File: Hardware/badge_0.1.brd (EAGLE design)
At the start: 100 x 50 mm, 60 parts, among them CON1 PH_2, IC1 CP2102, SW2 MK12C02, U1 SMBT2222A, U2 SMBT2222A, U4 MCP73832T-2DCI/OT

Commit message: okey dokey
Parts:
- removed R2, R3: 12K, SparkFun-Passives:0805
- removed U1, U2: SMBT2222A, badge:SOT95P290X110-3N
- added IC2: PIMH9, badge:SOT457
- added J7: 2X6 FEMALE, SparkFun-Connectors:2X6
- added JP2, JP3, JP4, JP6: JUMPER-PAD-2-NOJELLY, SparkFun-Passives:JELLYPAD-JUMPER-2-NO_NO_SILK
- J1: device SparkFun-Connectors:1X04 -> SparkFun-Connectors:1X03
- JP1: value (none) -> JUMPER-PAD-2-NOJELLY; device pinhead:1X06 -> SparkFun-Passives:JELLYPAD-JUMPER-2-NO_NO_SILK
- moved JP1 6.16 mm to (44.7, 35.6)
- moved D1 2.06 mm to (56.8, 44.8)
- moved C3 1.83 mm to (54.4, 8.57)
- moved IC1 1.75 mm to (52.4, 13.6)
- moved U$11 1.35 mm to (59.5, 37.0)
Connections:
- removed net N$10: R2.1, U1.1
- removed net N$3: R3.1, U2.1
- removed net S_!SUSP: IC1.11, J1.4
- new net DTR: IC2.P$2, IC2.P$4, J7.12, JP1.1
- new net RTS: IC2.P$1, IC2.P$5, J7.6, JP6.1
- new net S_RX: IC1.25, J2.6, J7.9, JP2.2
- new net S_TX: IC1.26, J2.5, J7.7, JP3.2
- net 5V: now also J7.4, JP4.2
- net GND: now also J7.1, J7.2; no longer JP1.1
- net GPIO0: now also IC2.P$3; no longer U1.3
- net RESET: now also IC2.P$6; no longer U2.3
- net RX: now also J7.8, JP3.1; no longer IC1.25, J2.6, JP1.4
- net S_DTR: now also J7.11, JP1.2; no longer JP1.6, R3.2, U1.2
- net S_RTS: now also J7.5, JP6.2; no longer JP1.3, R2.2, U2.2
- net TX: now also J7.10, JP2.1; no longer IC1.26, J2.5, JP1.5
- net VBUS: now also J7.3, JP4.1; no longer JP1.2
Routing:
- net S_TX: track 0.00 -> 48.5 mm, vias 0 -> 3
- net S_RX: track 0.00 -> 46.8 mm, vias 0 -> 4
- net RX: track 131.5 -> 84.9 mm, vias 6 -> 3
- net TX: track 133.2 -> 88.2 mm, vias 5 -> 2
- net RTS: track 0.00 -> 19.5 mm, vias 0 -> 1
- net S_RTS: track 68.5 -> 49.5 mm
- net DTR: track 0.00 -> 14.7 mm
- net S_DTR: track 57.1 -> 47.7 mm, vias 2 -> 3
- net VBUS: track 73.7 -> 81.7 mm, vias 7 -> 9
- net S_!SUSP: track 6.47 -> 0.00 mm
- net GND: track 380.6 -> 375.4 mm
- net N$3: track 4.74 -> 0.00 mm
- net N$10: track 4.48 -> 0.00 mm
- net S_SUSP: track 9.45 -> 6.38 mm
- net GPIO16: track 36.2 -> 34.2 mm
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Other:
- board text added: "BRT"
- board text removed: "!SUSP"
- board text removed: "2x12k"

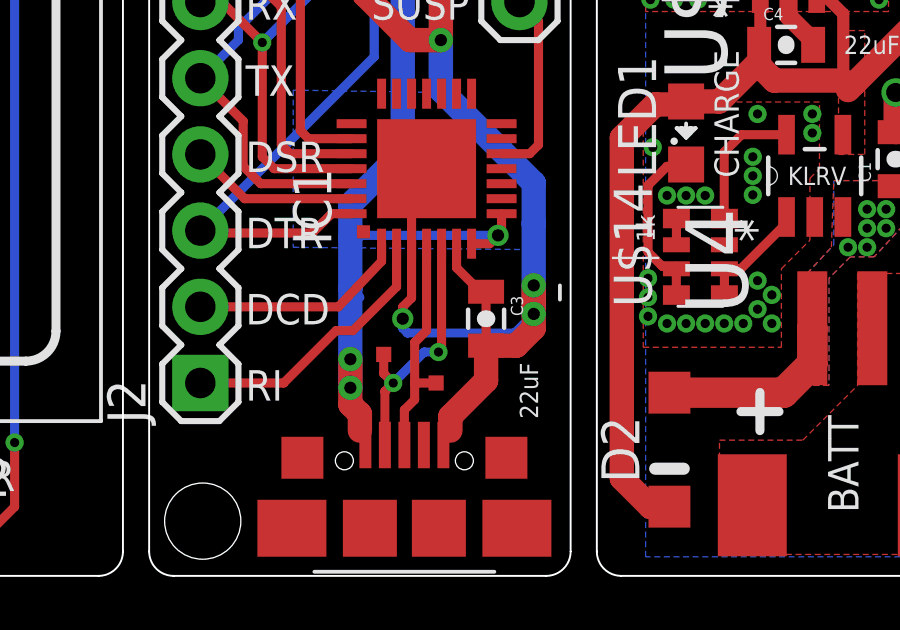
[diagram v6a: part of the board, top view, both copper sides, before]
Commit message: Fixed VBUS short-circuit overlap on CP2102 breakout
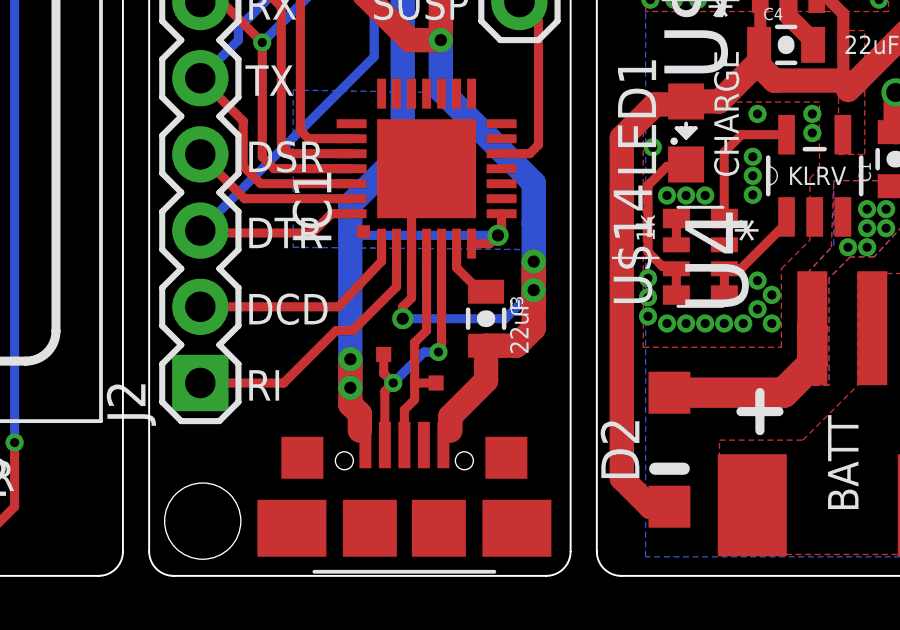
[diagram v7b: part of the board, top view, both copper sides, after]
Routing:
- net N$20: track 3.73 -> 2.12 mm
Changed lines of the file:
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@@
 <?xml version="1.0" encoding="utf-8"?>
 <!DOCTYPE eagle SYSTEM "eagle.dtd">
-<eagle version="7.5.0">
+<eagle version="7.1.0">
 <drawing>
 <settings>
@@
 <text x="51.435" y="35.2425" size="1.016" layer="21" font="vector" align="center-left">DTR</text>
 <text x="51.435" y="42.8625" size="1.016" layer="21" font="vector" align="center-left">RTS</text>
-<text x="55.800625" y="5.23875" size="0.6096" layer="21" font="vector" rot="R90" align="center-left">22uF</text>
-<wire x1="56.8325" y1="9.2075" x2="56.8325" y2="9.68375" width="0.127" layer="21"/>
+<text x="55.483125" y="7.381875" size="0.6096" layer="21" font="vector" rot="R90" align="center-left">22uF</text>
 <text x="92.80921875" y="5.9134375" size="1.27" layer="22" font="vector" rot="SMR270" align="center-left">TX</text>
 <text x="90.26921875" y="5.9134375" size="1.27" layer="22" font="vector" rot="SMR270" align="center-left">RX</text>
@@
 <wire x1="52.86375" y1="17.859375" x2="52.86375" y2="16.1925" width="0.8128" layer="16"/>
 <wire x1="52.86375" y1="16.1925" x2="55.959375" y2="13.096875" width="0.8128" layer="16"/>
-<via x="55.959375" y="8.73125" extent="1-16" drill="0.4064" diameter="0.8128" shape="octagon"/>
-<wire x1="55.959375" y1="9.68375" x2="55.959375" y2="8.73125" width="0.8128" layer="16"/>
-<wire x1="55.959375" y1="8.73125" x2="55.959375" y2="9.68375" width="0.8128" layer="1"/>
-<via x="55.959375" y="9.68375" extent="1-16" drill="0.4064" diameter="0.8128" shape="octagon"/>
+<via x="55.959375" y="9.525" extent="1-16" drill="0.4064" diameter="0.8128" shape="octagon"/>
+<wire x1="55.959375" y1="10.4775" x2="55.959375" y2="9.525" width="0.8128" layer="16"/>
+<wire x1="55.959375" y1="9.525" x2="55.959375" y2="10.4775" width="0.8128" layer="1"/>
+<via x="55.959375" y="10.4775" extent="1-16" drill="0.4064" diameter="0.8128" shape="octagon"/>
 <via x="52.86375" y="20.32" extent="1-16" drill="0.4064" diameter="0.8128" shape="octagon"/>
 <via x="52.86375" y="17.859375" extent="1-16" drill="0.4064" diameter="0.8128" shape="octagon"/>
@@
 <wire x1="73.81875" y1="41.9275" x2="74.3775" y2="42.48625" width="0.8128" layer="1"/>
 <wire x1="55.959375" y1="13.096875" x2="55.959375" y2="11.7475" width="0.8128" layer="16"/>
-<wire x1="55.959375" y1="11.7475" x2="55.959375" y2="9.68375" width="0.8128" layer="16"/>
+<wire x1="55.959375" y1="11.7475" x2="55.959375" y2="10.4775" width="0.8128" layer="16"/>
 <wire x1="52.86375" y1="20.32" x2="54.213125" y2="21.669375" width="0.8128" layer="1"/>
 <wire x1="54.213125" y1="21.669375" x2="55.483125" y2="21.669375" width="0.8128" layer="1"/>
@@
 <wire x1="51.59375" y1="8.969375" x2="51.59375" y2="8.5725" width="0.3048" layer="1"/>
 <via x="51.59375" y="8.5725" extent="1-16" drill="0.4064" shape="octagon"/>
-<wire x1="51.59375" y1="8.5725" x2="51.59375" y2="8.255" width="0.3048" layer="16"/>
-<wire x1="51.59375" y1="8.255" x2="51.7525" y2="8.09625" width="0.3048" layer="16"/>
-<wire x1="55.88" y1="8.651875" x2="55.959375" y2="8.73125" width="0.3048" layer="16"/>
+<wire x1="55.88" y1="9.445625" x2="55.959375" y2="9.525" width="0.3048" layer="16"/>
 <wire x1="51.8875" y1="11.073125" x2="51.8875" y2="12.914375" width="0.3048" layer="1"/>
 <wire x1="51.8875" y1="12.914375" x2="52.04625" y2="13.073125" width="0.3048" layer="1"/>
-<wire x1="55.959375" y1="8.73125" x2="55.959375" y2="8.255" width="0.8128" layer="1"/>
-<wire x1="55.959375" y1="8.255" x2="55.376875" y2="7.6725" width="0.8128" layer="1"/>
+<wire x1="55.959375" y1="9.525" x2="55.959375" y2="9.04875" width="0.8128" layer="1"/>
 <wire x1="54.371875" y1="7.6725" x2="55.376875" y2="7.6725" width="0.8128" layer="1"/>
 <wire x1="54.371875" y1="7.6725" x2="54.371875" y2="6.50875" width="0.8128" layer="1"/>
@@
 <wire x1="52.948125" y1="4.3625" x2="52.948125" y2="4.60875" width="0.3048" layer="1"/>
 <wire x1="52.948125" y1="4.60875" x2="53.18125" y2="4.841875" width="0.3048" layer="1"/>
-<wire x1="51.7525" y1="8.09625" x2="55.324375" y2="8.09625" width="0.3048" layer="16"/>
-<wire x1="55.324375" y1="8.09625" x2="55.959375" y2="8.73125" width="0.3048" layer="16"/>
 <wire x1="51.59375" y1="8.969375" x2="51.8875" y2="9.263125" width="0.3048" layer="1"/>
+<wire x1="55.376875" y1="7.6725" x2="55.959375" y2="8.255" width="0.8128" layer="1"/>
+<wire x1="55.959375" y1="8.255" x2="55.959375" y2="9.525" width="0.8128" layer="1"/>
+<wire x1="51.59375" y1="8.5725" x2="55.006875" y2="8.5725" width="0.3048" layer="16"/>
+<wire x1="55.006875" y1="8.5725" x2="55.959375" y2="9.525" width="0.3048" layer="16"/>
 </signal>
 <signal name="GPIO12/SPI_SO">
@@
 <wire x1="36.98875" y1="40.401875" x2="38.89375" y2="38.496875" width="0.8128" layer="16"/>
 <wire x1="52.943125" y1="24.209375" x2="55.483125" y2="24.209375" width="0.8128" layer="16"/>
-<wire x1="49.8475" y1="6.270625" x2="49.8475" y2="9.604375" width="0.8128" layer="16"/>
-<wire x1="49.8475" y1="9.604375" x2="49.8475" y2="11.27125" width="0.8128" layer="16"/>
+<wire x1="49.8475" y1="6.270625" x2="49.8475" y2="11.27125" width="0.8128" layer="16"/>
 <wire x1="49.8475" y1="11.27125" x2="49.8475" y2="12.3825" width="0.8128" layer="16"/>
 <wire x1="49.8475" y1="12.3825" x2="51.59375" y2="14.12875" width="0.8128" layer="16"/>
@@
 <wire x1="49.8475" y1="5.715" x2="50.165" y2="5.3975" width="0.8128" layer="1"/>
 <wire x1="50.165" y1="5.3975" x2="50.165" y2="4.841875" width="0.8128" layer="1"/>
-<wire x1="50.165" y1="9.286875" x2="49.8475" y2="9.604375" width="0.3048" layer="16"/>
 <contactref element="J7" pad="3"/>
 <contactref element="JP4" pad="1"/>
@@
 <contactref element="IC1" pad="6"/>
 <contactref element="C3" pad="1"/>
-<wire x1="54.371875" y1="7.858125" x2="54.371875" y2="9.4725" width="0.3048" layer="1"/>
 <wire x1="53.3875" y1="11.073125" x2="53.3875" y2="10.27125" width="0.3048" layer="1"/>
 <wire x1="53.3875" y1="10.27125" x2="54.18625" y2="9.4725" width="0.3048" layer="1"/>

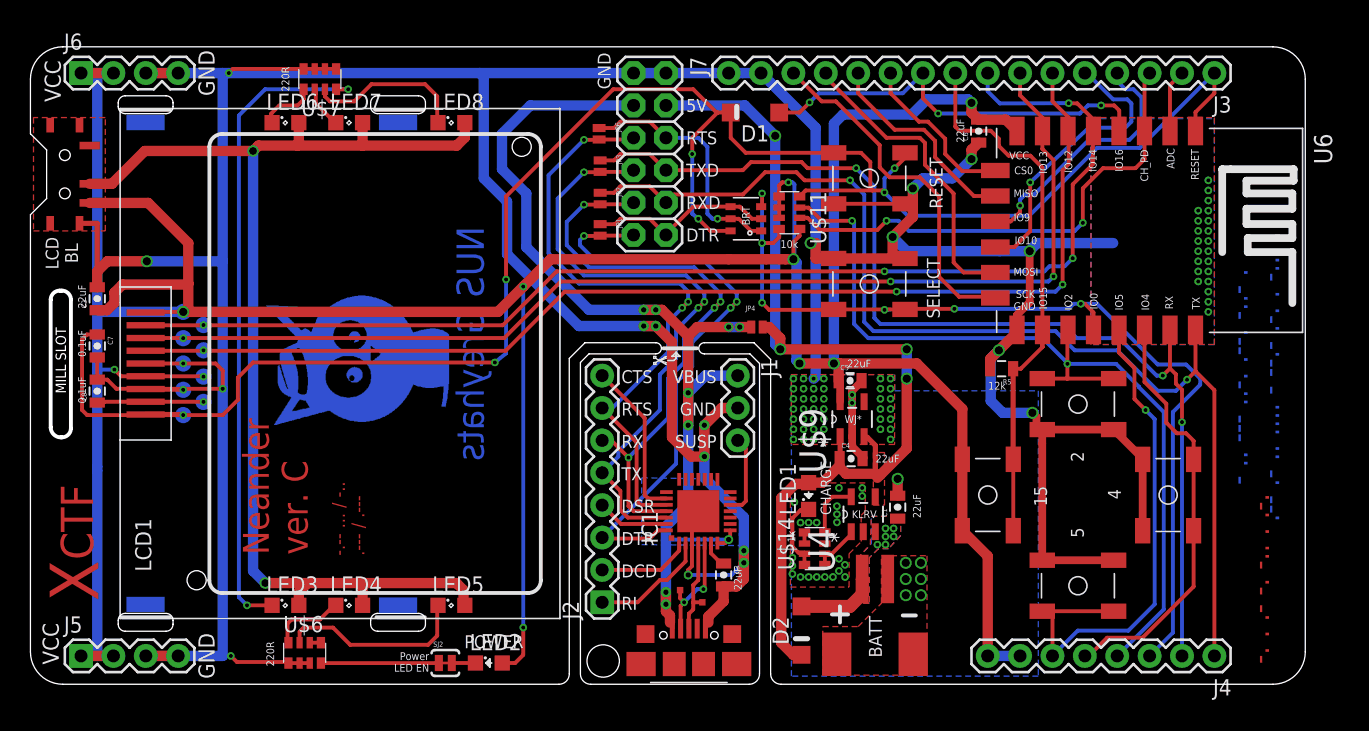
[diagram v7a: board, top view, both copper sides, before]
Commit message: All text back to vector for CAM, minor edits to some routing
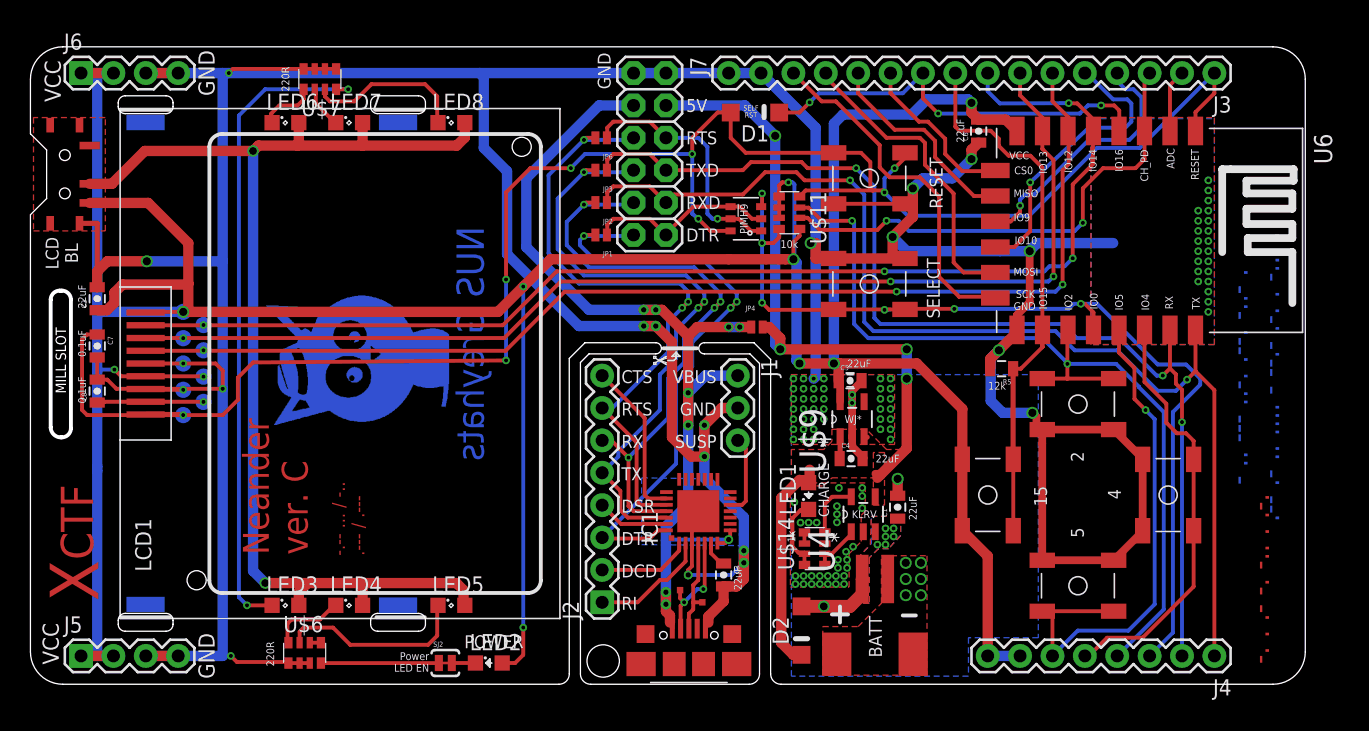
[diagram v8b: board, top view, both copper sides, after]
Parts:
- moved JP1 0.40 mm to (44.8, 35.2), turned to 180 degrees
- moved JP6 0.35 mm to (44.8, 42.9), turned to 180 degrees
- moved JP2 0.33 mm to (44.8, 37.8), turned to 180 degrees
- moved JP3 0.33 mm to (44.8, 40.3), turned to 180 degrees
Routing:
- net 5V: track 79.6 -> 70.1 mm
- net VBUS: track 81.2 -> 76.5 mm
- net RESET: track 155.2 -> 150.9 mm, vias 7 -> 8
- net GND: track 375.6 -> 378.8 mm, vias 113 -> 121
- net S_RX: track 46.8 -> 47.9 mm
- net S_RTS: track 49.5 -> 50.6 mm
- net S_DTR: track 47.7 -> 48.7 mm
- net S_TX: track 48.5 -> 49.5 mm
- net VBAT: vias 6 -> 7
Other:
- board text added: "PIM!H9"
- board text added: "SELF RST"
- board text removed: "BRT"
